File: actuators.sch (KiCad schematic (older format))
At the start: 52 parts, among them Q1 MBT3904DW1T1, Q2 MBT3904DW1T1, Q3 MBT3904DW1T1, Q4 MBT3904DW1T1, Q5 MBT3904DW1T1, U6 PCA9685

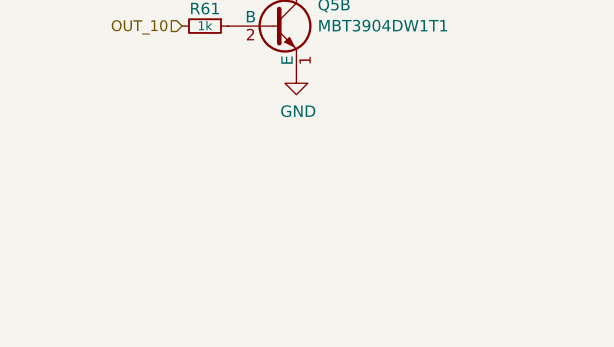
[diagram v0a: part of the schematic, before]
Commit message: Add CVRA logo to schematic
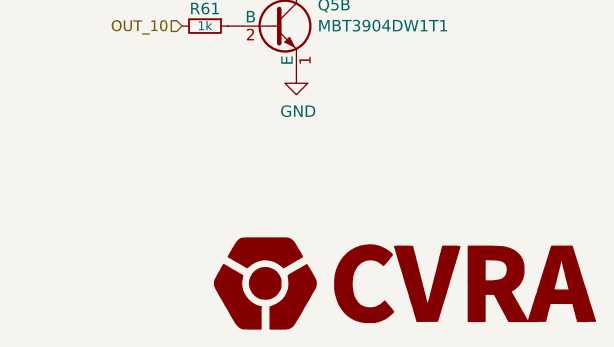
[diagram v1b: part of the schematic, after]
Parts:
- CONN17, CONN18, CONN19, CONN20, CONN25, CONN26, CONN31, CONN32, CONN37, CONN38: footprint (none) -> Pin_Headers:Pin_Header_Straight_1x02
- CONN21, CONN22, CONN23, CONN24, CONN27, CONN28, CONN29, CONN30, CONN33, CONN34, CONN35, CONN36, CONN39: footprint (none) -> Pin_Headers:Pin_Header_Straight_1x03
- CONN40: footprint (none) -> Pin_Headers:Pin_Header_Straight_1x04
- R43, R44, R45, R46, R47, R48, R49, R50, R51, R52, R53, R54, R55, R56, R57, R58, R59, R60, R61, R62, R63: footprint (none) -> _std:_0603

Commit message: Associate footprints
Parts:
- CONN17, CONN18, CONN19, CONN20, CONN25, CONN26, CONN31, CONN32, CONN37, CONN38: footprint Pin_Headers:Pin_Header_Straight_1x02 -> _connectors:_Pin2mm_2
- CONN40: footprint Pin_Headers:Pin_Header_Straight_1x04 -> _connectors:_Pin2mm_4
- Q1, Q2, Q3, Q4, Q5: footprint (none) -> _std:SOT363
- U6: footprint (none) -> Housings_SSOP:TSSOP-28_4.4x9.7mm_Pitch0.65mm
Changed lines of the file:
@@
 F 0 "U6" H 2600 950 39  0000 C CNN
 F 1 "PCA9685" H 2300 2750 39  0000 C CNN
-F 2 "" H 2300 1950 39  0001 C CNN
+F 2 "Housings_SSOP:TSSOP-28_4.4x9.7mm_Pitch0.65mm" H 2300 1950 39  0001 C CNN
 F 3 "" H 2300 1950 39  0000 C CNN
 	1    2300 1950
@@
 F 0 "Q1" H 1543 4367 50  0000 L CNN
 F 1 "MBT3904DW1T1" H 1543 4275 50  0000 L CNN
-F 2 "" H 1543 4183 50  0001 L CIN
+F 2 "_std:SOT363" H 1543 4183 50  0001 L CIN
 F 3 "" H 1350 4275 50  0000 L CNN
 	1    1350 4275
@@
 F 0 "Q1" H 1543 5817 50  0000 L CNN
 F 1 "MBT3904DW1T1" H 1543 5725 50  0000 L CNN
-F 2 "" H 1543 5633 50  0001 L CIN
+F 2 "_std:SOT363" H 1543 5633 50  0001 L CIN
 F 3 "" H 1350 5725 50  0000 L CNN
 	2    1350 5725
@@
 F 0 "Q2" H 3618 4367 50  0000 L CNN
 F 1 "MBT3904DW1T1" H 3618 4275 50  0000 L CNN
-F 2 "" H 3618 4183 50  0001 L CIN
+F 2 "_std:SOT363" H 3618 4183 50  0001 L CIN
 F 3 "" H 3425 4275 50  0000 L CNN
 	1    3425 4275
@@
 F 0 "Q2" H 3618 5792 50  0000 L CNN
 F 1 "MBT3904DW1T1" H 3618 5700 50  0000 L CNN
-F 2 "" H 3618 5608 50  0001 L CIN
+F 2 "_std:SOT363" H 3618 5608 50  0001 L CIN
 F 3 "" H 3425 5700 50  0000 L CNN
 	2    3425 5700
@@
 F 0 "Q3" H 5693 4367 50  0000 L CNN
 F 1 "MBT3904DW1T1" H 5693 4275 50  0000 L CNN
-F 2 "" H 5693 4183 50  0001 L CIN
+F 2 "_std:SOT363" H 5693 4183 50  0001 L CIN
 F 3 "" H 5500 4275 50  0000 L CNN
 	1    5500 4275
@@
 F 0 "Q3" H 5693 5792 50  0000 L CNN
 F 1 "MBT3904DW1T1" H 5693 5700 50  0000 L CNN
-F 2 "" H 5693 5608 50  0001 L CIN
+F 2 "_std:SOT363" H 5693 5608 50  0001 L CIN
 F 3 "" H 5500 5700 50  0000 L CNN
 	2    5500 5700
@@
 F 0 "Q4" H 7768 4367 50  0000 L CNN
 F 1 "MBT3904DW1T1" H 7768 4275 50  0000 L CNN
-F 2 "" H 7768 4183 50  0001 L CIN
+F 2 "_std:SOT363" H 7768 4183 50  0001 L CIN
 F 3 "" H 7575 4275 50  0000 L CNN
 	1    7575 4275
@@
 F 0 "Q4" H 7768 5792 50  0000 L CNN
 F 1 "MBT3904DW1T1" H 7768 5700 50  0000 L CNN
-F 2 "" H 7768 5608 50  0001 L CIN
+F 2 "_std:SOT363" H 7768 5608 50  0001 L CIN
 F 3 "" H 7575 5700 50  0000 L CNN
 	2    7575 5700
@@
 F 0 "Q5" H 9843 4367 50  0000 L CNN
 F 1 "MBT3904DW1T1" H 9843 4275 50  0000 L CNN
-F 2 "" H 9843 4183 50  0001 L CIN
+F 2 "_std:SOT363" H 9843 4183 50  0001 L CIN
 F 3 "" H 9650 4275 50  0000 L CNN
 	1    9650 4275
@@
 F 0 "Q5" H 9843 5792 50  0000 L CNN
 F 1 "MBT3904DW1T1" H 9843 5700 50  0000 L CNN
-F 2 "" H 9843 5608 50  0001 L CIN
+F 2 "_std:SOT363" H 9843 5608 50  0001 L CIN
 F 3 "" H 9650 5700 50  0000 L CNN
 	2    9650 5700
@@
 F 0 "CONN17" H 2078 3977 59  0000 L CNN
 F 1 "LOAD" H 2078 3873 59  0000 L CNN
-F 2 "Pin_Headers:Pin_Header_Straight_1x02" H 1900 3875 59  0001 C CNN
+F 2 "_connectors:_Pin2mm_2" H 1900 3875 59  0001 C CNN
 F 3 "" H 1900 3875 59  0000 C CNN
 	1    1900 3925
@@
 F 0 "CONN18" H 2078 5402 59  0000 L CNN
 F 1 "LOAD" H 2078 5298 59  0000 L CNN
-F 2 "Pin_Headers:Pin_Header_Straight_1x02" H 1900 5300 59  0001 C CNN
+F 2 "_connectors:_Pin2mm_2" H 1900 5300 59  0001 C CNN
 F 3 "" H 1900 5300 59  0000 C CNN
 	1    1900 5350
@@
 F 0 "CONN19" H 4153 3977 59  0000 L CNN
 F 1 "LOAD" H 4153 3873 59  0000 L CNN
-F 2 "Pin_Headers:Pin_Header_Straight_1x02" H 3975 3875 59  0001 C CNN
+F 2 "_connectors:_Pin2mm_2" H 3975 3875 59  0001 C CNN
 F 3 "" H 3975 3875 59  0000 C CNN
 	1    3975 3925
@@
 F 0 "CONN20" H 4153 5402 59  0000 L CNN
 F 1 "LOAD" H 4153 5298 59  0000 L CNN
-F 2 "Pin_Headers:Pin_Header_Straight_1x02" H 3975 5300 59  0001 C CNN
+F 2 "_connectors:_Pin2mm_2" H 3975 5300 59  0001 C CNN
 F 3 "" H 3975 5300 59  0000 C CNN
 	1    3975 5350
@@
 F 0 "CONN26" H 6228 5402 59  0000 L CNN
 F 1 "LOAD" H 6228 5298 59  0000 L CNN
-F 2 "Pin_Headers:Pin_Header_Straight_1x02" H 6050 5300 59  0001 C CNN
+F 2 "_connectors:_Pin2mm_2" H 6050 5300 59  0001 C CNN
 F 3 "" H 6050 5300 59  0000 C CNN
 	1    6050 5350
@@
 F 0 "CONN32" H 8303 5402 59  0000 L CNN
 F 1 "LOAD" H 8303 5298 59  0000 L CNN
-F 2 "Pin_Headers:Pin_Header_Straight_1x02" H 8125 5300 59  0001 C CNN
+F 2 "_connectors:_Pin2mm_2" H 8125 5300 59  0001 C CNN
 F 3 "" H 8125 5300 59  0000 C CNN
 	1    8125 5350
@@
 F 0 "CONN25" H 6228 3977 59  0000 L CNN
 F 1 "LOAD" H 6228 3873 59  0000 L CNN
-F 2 "Pin_Headers:Pin_Header_Straight_1x02" H 6050 3875 59  0001 C CNN
+F 2 "_connectors:_Pin2mm_2" H 6050 3875 59  0001 C CNN
 F 3 "" H 6050 3875 59  0000 C CNN
 	1    6050 3925
@@
 F 0 "CONN31" H 8303 3977 59  0000 L CNN
 F 1 "LOAD" H 8303 3873 59  0000 L CNN
-F 2 "Pin_Headers:Pin_Header_Straight_1x02" H 8125 3875 59  0001 C CNN
+F 2 "_connectors:_Pin2mm_2" H 8125 3875 59  0001 C CNN
 F 3 "" H 8125 3875 59  0000 C CNN
 	1    8125 3925
@@
 F 0 "CONN37" H 10378 3977 59  0000 L CNN
 F 1 "LOAD" H 10378 3873 59  0000 L CNN
-F 2 "Pin_Headers:Pin_Header_Straight_1x02" H 10200 3875 59  0001 C CNN
+F 2 "_connectors:_Pin2mm_2" H 10200 3875 59  0001 C CNN
 F 3 "" H 10200 3875 59  0000 C CNN
 	1    10200 3925
@@
 F 0 "CONN38" H 10378 5402 59  0000 L CNN
 F 1 "LOAD" H 10378 5298 59  0000 L CNN
-F 2 "Pin_Headers:Pin_Header_Straight_1x02" H 10200 5300 59  0001 C CNN
+F 2 "_connectors:_Pin2mm_2" H 10200 5300 59  0001 C CNN
 F 3 "" H 10200 5300 59  0000 C CNN
 	1    10200 5350
@@
 F 0 "CONN40" H 10628 2690 59  0000 L CNN
 F 1 "RGB" H 10628 2586 59  0000 L CNN
-F 2 "Pin_Headers:Pin_Header_Straight_1x04" H 10450 2375 59  0001 C CNN
+F 2 "_connectors:_Pin2mm_4" H 10450 2375 59  0001 C CNN
 F 3 "" H 10450 2375 59  0000 C CNN
 	1    10450 2375
@@
 $EndComp
 $Comp
-L CVRA_logo #G?
+L CVRA_logo #G3
 U 1 1 56D2205D
 P 10225 6825
-F 0 "#G?" H 10225 6657 60  0001 C CNN
+F 0 "#G3" H 10225 6657 60  0001 C CNN
 F 1 "CVRA_logo" H 10225 6993 60  0001 C CNN
 F 2 "" H 10225 6825 60  0000 C CNN

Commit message: Place components on PCB
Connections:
- net at Q1.6 (C): now also CONN18.2 (OUT-)
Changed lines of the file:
@@
 	1550 5400 1450 5400
 Wire Wire Line
-	1450 5400 1450 5500
+	1450 5400 1450 5525
 Wire Wire Line
 	1450 5225 1450 5300
